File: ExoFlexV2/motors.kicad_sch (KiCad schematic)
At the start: 9 parts

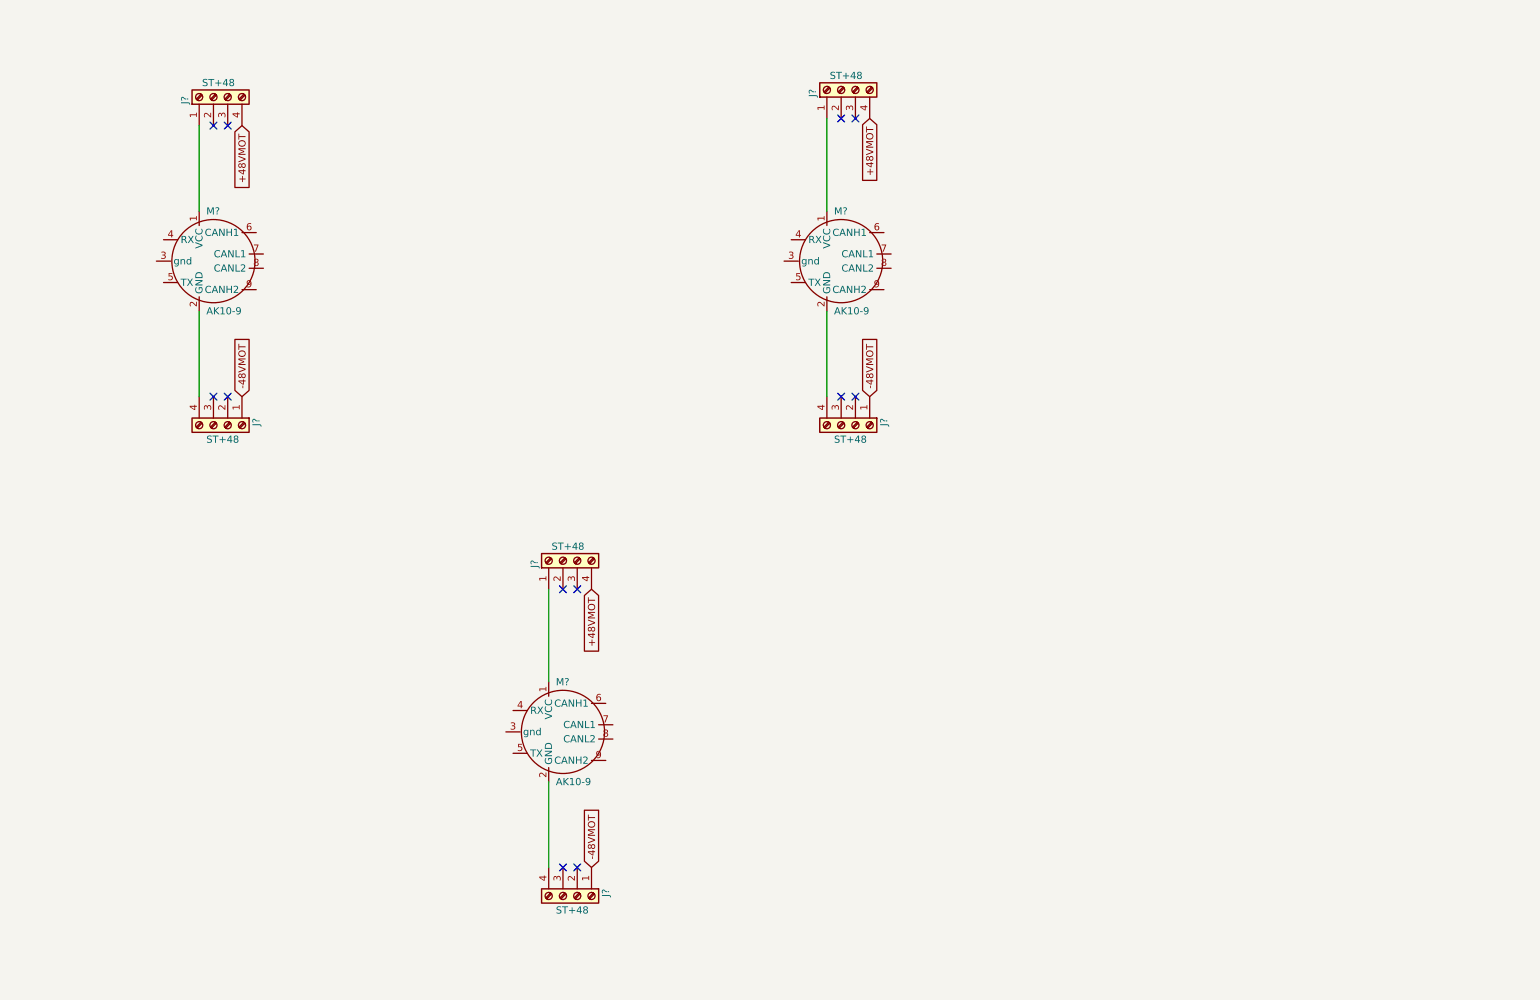
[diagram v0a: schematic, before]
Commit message: Many changes
Debouncing, power protection, potentiometer limits, etc.
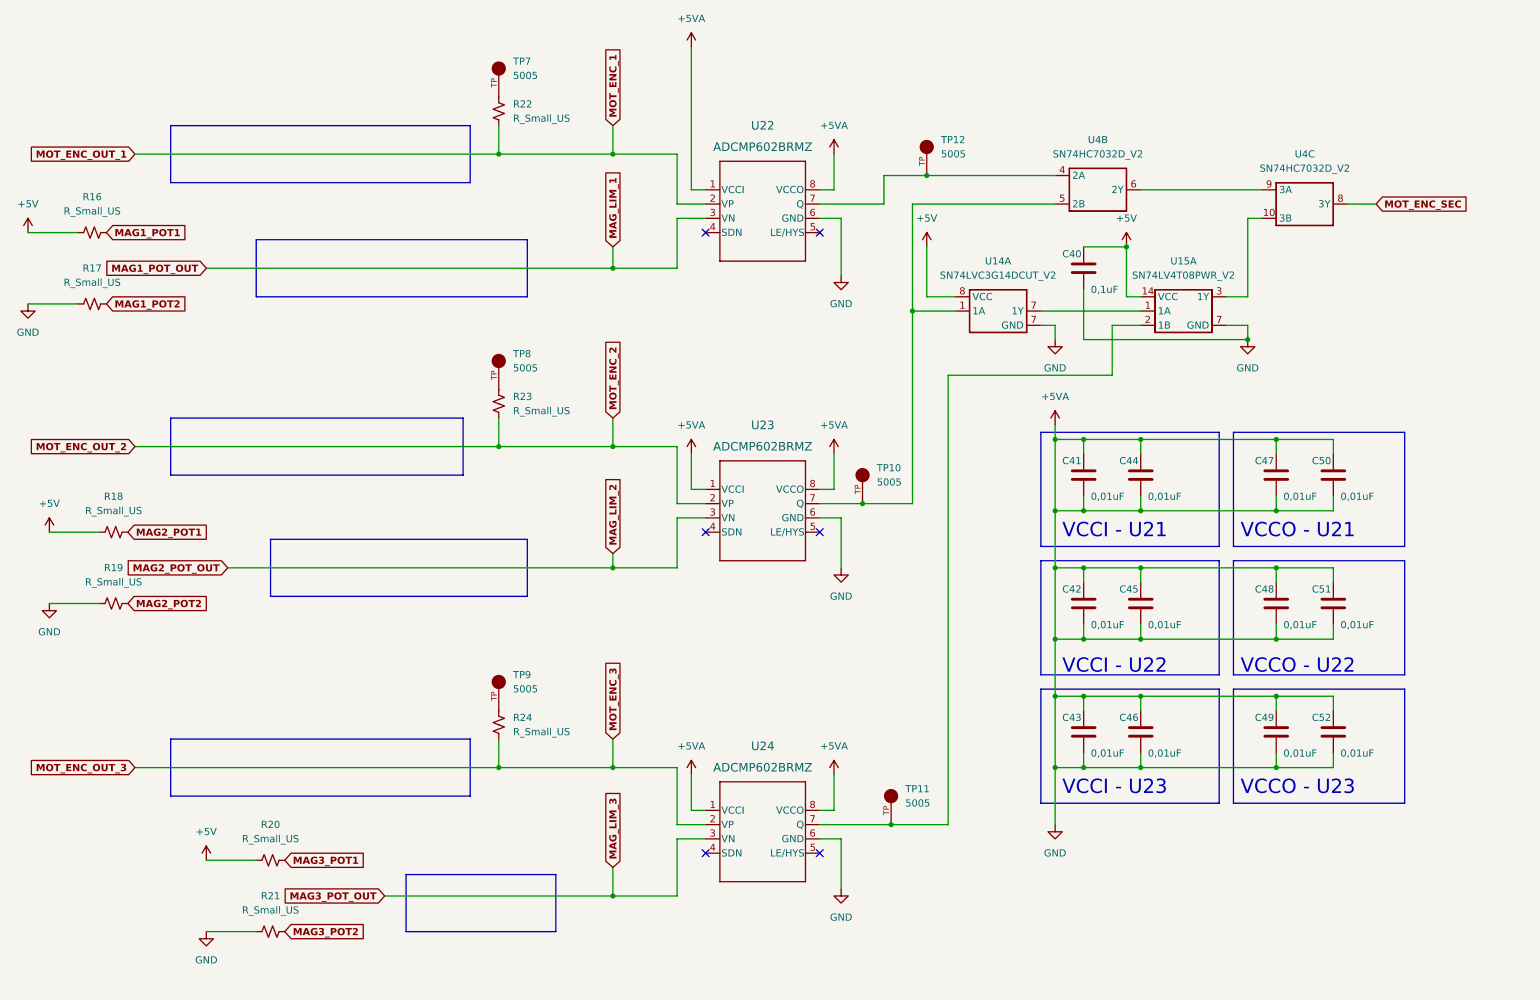
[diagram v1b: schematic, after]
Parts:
- removed J? (x6): ST+48, symbol Connector:Screw_Terminal_01x04
- removed M? (x3): AK10-9, symbol SymLib:AK10-9
- added C40: 0,1uF, Capacitor_SMD:C_0603_1608Metric, symbol Device:C
- added C41, C42, C43, C44, C45, C46, C47, C48, C49, C50, C51, C52: 0,01uF, Capacitor_SMD:C_0603_1608Metric, symbol Device:C
- added R16, R17, R18, R19, R20, R21, R22, R23, R24: R_Small_US, Resistor_SMD:R_0603_1608Metric, symbol Device:R_Small_US
- added TP10, TP11, TP12, TP7, TP8, TP9: 5005, FootPrint:KEYSTONE_5005, symbol SymLib:5005
- added U14: SN74LVC3G14DCUT_V2, FootPrint:SN74LVC3G14DCUT, symbol SymLib:SN74LVC3G14DCUT_V2
- added U15: SN74LV4T08PWR_V2, FootPrint:SN74LV4T08PWR, symbol SymLib:SN74LV4T08PWR_V2
- added U22, U23, U24: ADCMP602BRMZ, FootPrint:ADCMP602BRMZ, symbol SymLib:ADCMP602BRMZ
- added U4: SN74HC7032D_V2, FootPrint:SN74HC7032D, symbol SymLib:SN74HC7032D_V2
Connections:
- new net: TP12.TP, U22.7 (Q), U4.4 (2A)
- new net: R24.1, TP9.TP
- new net: TP10.TP, U14.1 (1A), U23.7 (Q), U4.5 (2B)
- new net: U4.6 (2Y), U4.9 (3A)
- new net: TP11.TP, U15.2 (1B), U24.7 (Q)
- new net: R23.1, TP8.TP
- new net: U14.7 (GND), U15.1 (1A)
- new net: U15.3 (1Y), U4.10 (3B)
- new net: R22.1, TP7.TP
- new net +5V: C40.1, R16.1, R18.1, R20.1, U14.8 (VCC), U15.14 (VCC)
- new net +5VA: C40.2, C41.1, C41.2, C42.1, C42.2, C43.1, C43.2, C44.1, C44.2, C45.1, C45.2, C46.1, C46.2, C47.1, C47.2, C48.1, C48.2, C49.1, C49.2, C50.1, C50.2, C51.1, C51.2, C52.1, C52.2, R17.1, R19.1, R21.1, U14.7 (GND), U15.7 (GND), U22.1 (VCCI), U22.6 (GND), U22.8 (VCCO), U23.1 (VCCI), U23.6 (GND), U23.8 (VCCO), U24.1 (VCCI), U24.6 (GND), U24.8 (VCCO)
- new net MAG1_POT1: R16.2
- new net MAG1_POT2: R17.2
- new net MAG1_POT_OUT: U22.3 (VN)
- new net MAG2_POT1: R18.2
- new net MAG2_POT2: R19.2
- new net MAG2_POT_OUT: U23.3 (VN)
- new net MAG3_POT1: R20.2
- new net MAG3_POT2: R21.2
- new net MAG3_POT_OUT: U24.3 (VN)
- new net MOT_ENC_1: R22.2, U22.2 (VP)
- new net MOT_ENC_2: R23.2, U23.2 (VP)
- new net MOT_ENC_3: R24.2, U24.2 (VP)
- new net MOT_ENC_SEC: U4.8 (3Y)
- no-connect marks 12 -> 6
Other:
- note added: "VCCI - U21"
- note added: "VCCI - U22"
- note added: "VCCI - U23"
- note added: "VCCO - U21"
- note added: "VCCO - U22"
- note added: "VCCO - U23"

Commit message: quque truc
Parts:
- removed R22, R23, R24: R_Small_US, Resistor_SMD:R_0603_1608Metric, symbol Device:R_Small_US
- removed TP7, TP8, TP9: 5005, FootPrint:KEYSTONE_5005, symbol SymLib:5005
- added C43, C44, C45, C46, C47, C48: 1nF, Capacitor_SMD:C_0603_1608Metric, symbol Device:C
- added R27, R28, R29: 0 ohm, Resistor_SMD:R_0603_1608Metric, symbol Device:R_Small_US
- added R30, R33, R34, R35, R36, R37: 7,5k, Resistor_SMD:R_0603_1608Metric, symbol Device:R_Small_US
- added TP20, TP21, TP22, TP23, TP24, TP25, TP26, TP27, TP31: 5005, FootPrint:KEYSTONE_5005, symbol SymLib:5005
- renumbered C40 to C49, C41 to C50, C42 to C51, C43 to C52, C44 to C53, C45 to C54, C46 to C55, C47 to C56, C48 to C57, C49 to C58, C50 to C59, C51 to C60, C52 to C61, R16 to R23, R17 to R24, R18 to R25, R19 to R26, R20 to R31, R21 to R32, TP10 to TP28, TP11 to TP29, TP12 to TP30, U14 to U15, U15 to U16, U22 to U21, U23 to U22, U24 to U23, U4 to U5
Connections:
- net +5V: no longer R23.1, R25.1, R31.1
- net +5VA: now also R23.1, R25.1, R31.1; no longer C49.2, C50.2, C51.2, C52.2, C53.2, C54.2, C55.2, C56.2, C57.2, C58.2, C59.2, C60.2, C61.2, R24.1, R26.1, R32.1, U15.7 (GND), U16.7 (GND), U21.6 (GND), U22.6 (GND), U23.6 (GND)
- net MAG1_POT_OUT: now also R34.1; no longer U21.3 (VN)
- net MAG2_POT_OUT: now also R35.1; no longer U22.3 (VN)
- net MAG3_POT_OUT: now also R37.1; no longer U23.3 (VN)
- net MOT_ENC_1: now also C44.1, R33.2, TP23.TP
- net MOT_ENC_2: now also C43.1, R30.2, TP25.TP
- net MOT_ENC_3: now also C47.1, R36.2
- net MOT_ENC_SEC: now also TP31.TP
- new net: R29.1, TP22.TP
- new net: R27.1, TP20.TP
- new net: R28.1, TP21.TP
- new net GND: C43.2, C44.2, C45.2, C46.2, C47.2, C48.2, C49.2, C50.2, C51.2, C52.2, C53.2, C54.2, C55.2, C56.2, C57.2, C58.2, C59.2, C60.2, C61.2, R24.1, R26.1, R32.1, U15.7 (GND), U16.7 (GND), U21.6 (GND), U22.6 (GND), U23.6 (GND)
- new net MAG_LIM_1: C45.1, R34.2, TP24.TP, U21.3 (VN)
- new net MAG_LIM_2: C46.1, R35.2, TP26.TP, U22.3 (VN)
- new net MAG_LIM_3: C48.1, R37.2, TP27.TP, U23.3 (VN)
- new net MOT_ENC_OUT_1: R27.2, R33.1
- new net MOT_ENC_OUT_2: R28.2, R30.1
- new net MOT_ENC_OUT_3: R29.2, R36.1

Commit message: Placement
Début du placement et modification d'après dernier review
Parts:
- removed R23, R24, R25, R26, R31, R32: R_Small_US, Resistor_SMD:R_0603_1608Metric, symbol Device:R_Small_US
- added TP51, TP56, TP57, TP58: 5005, FootPrint:KEYSTONE_5005, symbol SymLib:5005
- R28: renamed from R27; value 0 ohm -> 0Ω
- R29: renamed from R28; value 0 ohm -> 0Ω
- R30: renamed from R29; value 0 ohm -> 0Ω
- renumbered C44 to C47, C45 to C48, C43 to C49, C46 to C50, C47 to C51, C48 to C52, C49 to C53, C50 to C54, C51 to C55, C52 to C56, C53 to C57, C54 to C58, C55 to C59, C56 to C60, C57 to C61, C58 to C62, C59 to C63, C60 to C64, C61 to C65, R33 to R31, R34 to R32, R30 to R33, R35 to R34, R36 to R35, R37 to R36, TP20 to TP44, TP21 to TP45, TP22 to TP46, TP23 to TP47, TP24 to TP48, TP25 to TP49, TP26 to TP50, TP27 to TP52, TP28 to TP53, TP29 to TP54, TP30 to TP55, TP31 to TP59, U15 to U13, U5 to U14, U16 to U15
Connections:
- net MOT_ENC_3: now also TP51.TP
- net at U14.6 (2Y), U14.9 (3A): now also TP57.TP
- net at U13.7 (GND), U15.1 (1A): now also TP56.TP
- net at U14.10 (3B), U15.3 (1Y): now also TP58.TP
- net MAG_LIM_1: no longer names the net of C48.1, R32.2, TP48.TP, U21.3 (VN)
- net MAG_LIM_2: no longer names the net of C50.1, R34.2, TP50.TP, U22.3 (VN)
- net MAG_LIM_3: no longer names the net of C52.1, R36.2, TP52.TP, U23.3 (VN)
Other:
- moved on the sheet: C47, C48, C49, C50, C51, C52, R31, R32, R33, R34, R35, R36

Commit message: Placement encore
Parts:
- renumbered C47 to C48, C48 to C49, C49 to C50, C50 to C51, C51 to C52, C52 to C53, C53 to C54, C54 to C55, C55 to C56, C56 to C57, C57 to C58, C58 to C59, C59 to C60, C60 to C61, C61 to C62, C62 to C63, C63 to C64, C64 to C65, C65 to C66, R28 to R29, R29 to R30, R30 to R31, R31 to R32, R32 to R33, R33 to R34, R34 to R35, R35 to R36, R36 to R37, U13 to U14, U14 to U15, U15 to U16

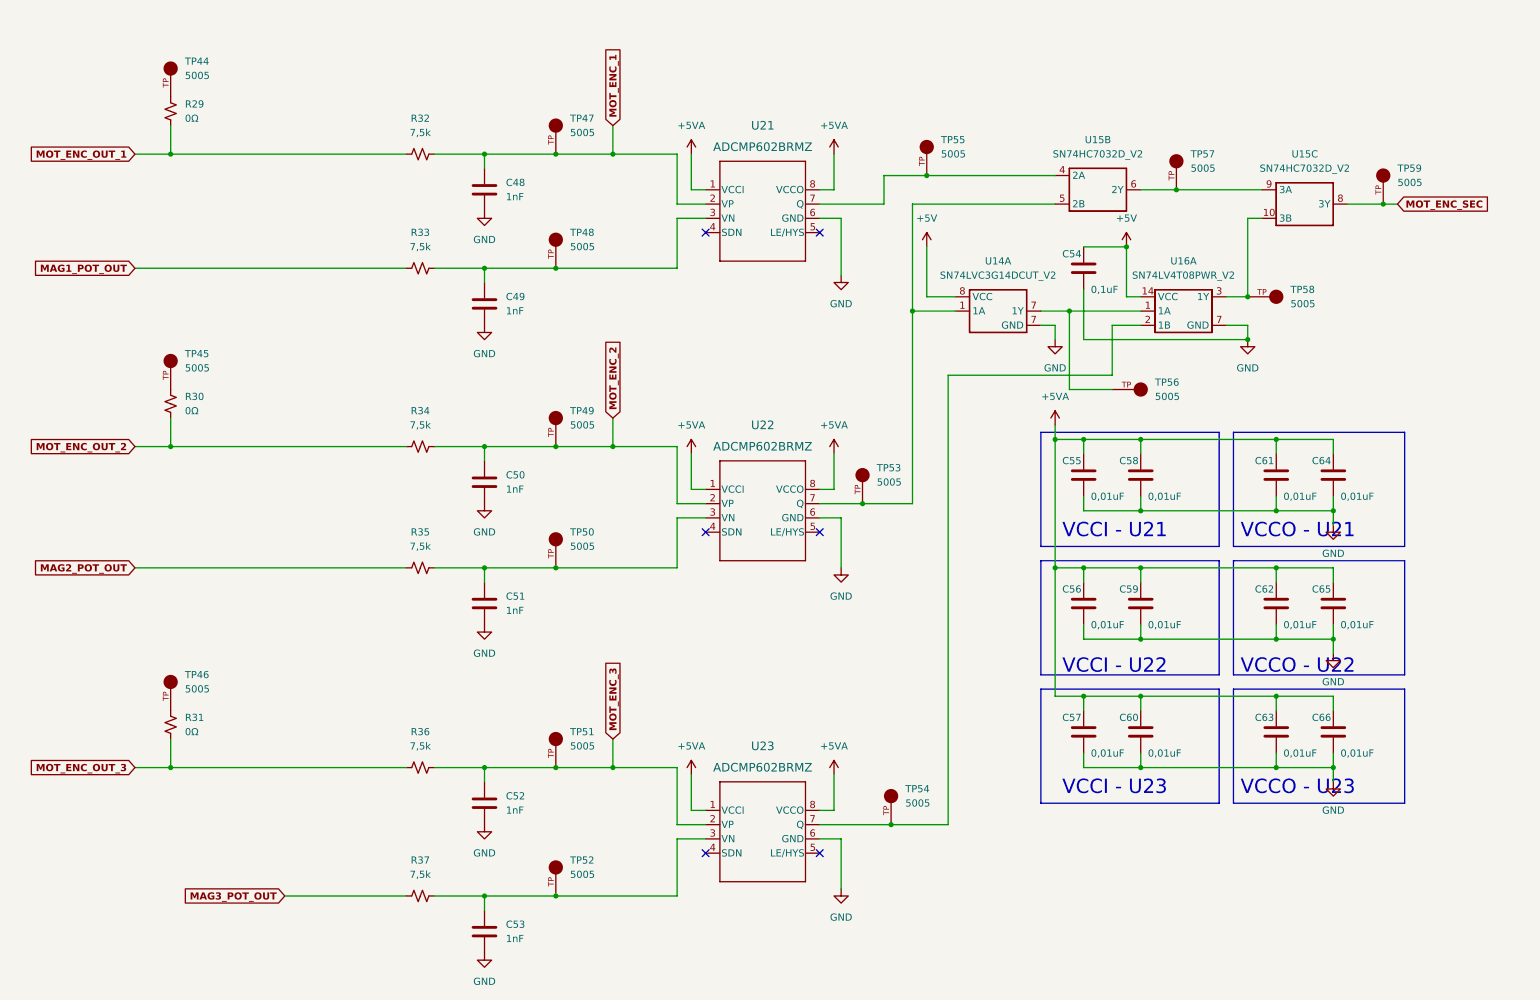
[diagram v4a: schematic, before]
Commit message: Mise à jour mi-stage
- Torque et Amplitude testé et vérifié
- Capteur de présence et de proximité testé
- Système de détection de coupure de fils
- Polyvalence pour plusieurs capteurs
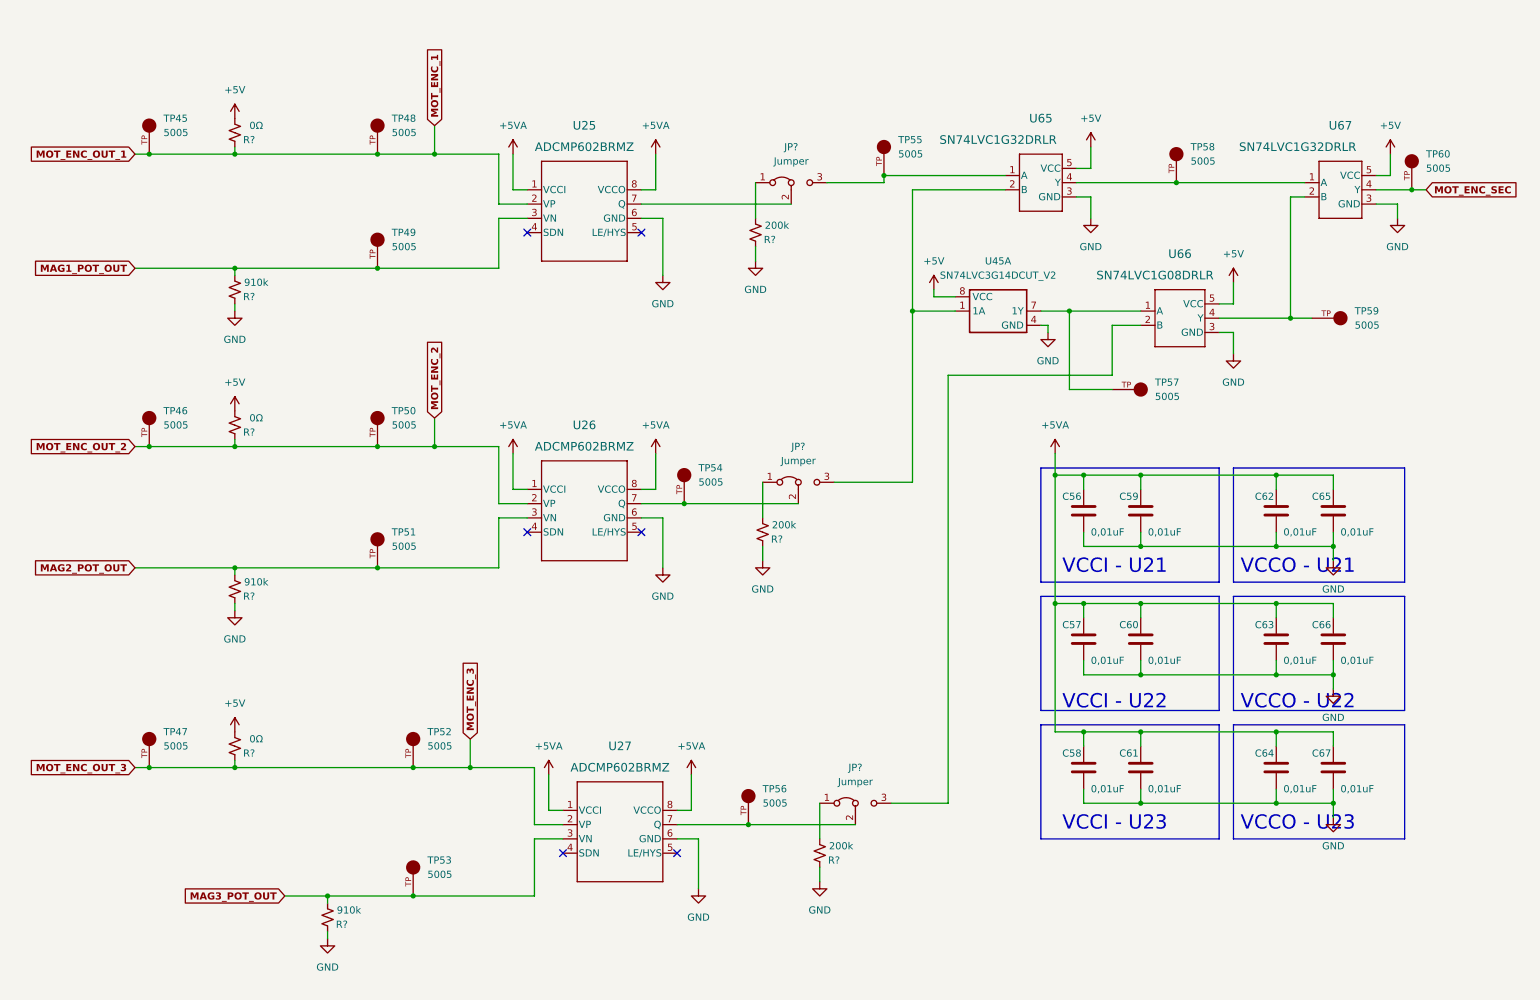
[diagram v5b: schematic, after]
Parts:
- removed C48, C49, C50, C51, C52, C53: 1nF, Capacitor_SMD:C_0603_1608Metric, symbol Device:C
- removed C54: 0,1uF, Capacitor_SMD:C_0603_1608Metric, symbol Device:C
- removed R29, R30, R31: 0Ω, Resistor_SMD:R_0603_1608Metric, symbol Device:R_Small_US
- removed R32, R33, R34, R35, R36, R37: 7,5k, Resistor_SMD:R_0603_1608Metric, symbol Device:R_Small_US
- removed U14: SN74LVC3G14DCUT_V2, FootPrint:SN74LVC3G14DCUT, symbol SymLib:SN74LVC3G14DCUT_V2
- removed U15: SN74HC7032D_V2, FootPrint:SN74HC7032D, symbol SymLib:SN74HC7032D_V2
- removed U16: SN74LV4T08PWR_V2, FootPrint:SN74LV4T08PWR, symbol SymLib:SN74LV4T08PWR_V2
- added JP? (x3): Jumper, Connector_PinHeader_2.54mm:PinHeader_1x03_P2.54mm_Vertical, symbol Jumper:Jumper_3_Bridged12
- added R? (x3): 910k, Resistor_SMD:R_1206_3216Metric_Pad1.30x1.75mm_HandSolder, symbol Device:R_Small_US
- added R? (x3): 200k, Resistor_SMD:R_0603_1608Metric, symbol Device:R_Small_US
- added R? (x3): 0Ω, Resistor_SMD:R_1206_3216Metric_Pad1.30x1.75mm_HandSolder, symbol Device:R_Small_US
- added U45: SN74LVC3G14DCUT_V2, FootPrint:SN74LVC3G14DCUT, symbol SymLib:SN74LVC3G14DCUT_V2
- added U65, U67: SN74LVC1G32DRLR, FootPrint:DRL5, symbol SymLib:SN74LVC1G32DRLR
- added U66: SN74LVC1G08DRLR, FootPrint:DRL5, symbol SymLib:SN74LVC1G08DRLR
- renumbered C55 to C56, C56 to C57, C57 to C58, C58 to C59, C59 to C60, C60 to C61, C61 to C62, C62 to C63, C63 to C64, C64 to C65, C65 to C66, C66 to C67, TP44 to TP45, TP45 to TP46, TP46 to TP47, TP47 to TP48, TP48 to TP49, TP49 to TP50, TP50 to TP51, TP51 to TP52, TP52 to TP53, TP53 to TP54, TP54 to TP56, TP56 to TP57, TP57 to TP58, TP58 to TP59, TP59 to TP60, U21 to U25, U22 to U26, U23 to U27
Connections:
- net +5V: now also R?.1, R?.1, R?.1, U45.8 (VCC), U65.5 (VCC), U66.5 (VCC), U67.5 (VCC)
- net GND: now also R?.2, R?.2, R?.2, R?.2, R?.2, R?.2, U45.4 (GND), U65.3 (GND), U66.3 (GND), U67.3 (GND)
- net MAG1_POT_OUT: now also TP49.TP, U25.3 (VN), R?.1
- net MAG2_POT_OUT: now also TP51.TP, U26.3 (VN), R?.1
- net MAG3_POT_OUT: now also TP53.TP, U27.3 (VN), R?.1
- net MOT_ENC_1: now also TP45.TP, R?.2
- net MOT_ENC_2: now also TP46.TP, R?.2
- net MOT_ENC_3: now also TP47.TP, R?.2
- net MOT_ENC_SEC: now also U67.4 (Y)
- net at TP57.TP: now also U45.7 (1Y), U66.1 (A)
- net at U25.7 (Q): now also JP?.2 (C); no longer TP55.TP
- net at TP54.TP, U26.7 (Q): now also JP?.2 (C)
- net at TP58.TP: now also U65.4 (Y), U67.1 (A)
- net at TP56.TP, U27.7 (Q): now also JP?.2 (C)
- net at TP59.TP: now also U66.4 (Y), U67.2 (B)
- new net: JP?.1 (A), R?.1 (x3)
- new net: JP?.3 (B), TP55.TP, U65.1 (A)
- new net: JP?.3 (B), U45.1 (1A), U65.2 (B)
- new net: JP?.3 (B), U66.2 (B)
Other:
- moved on the sheet: C56, C57, C58, C59, C60, C61, C62, C63, C64, C65, C66, C67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
